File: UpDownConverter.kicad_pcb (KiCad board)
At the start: 4 copper layers, 92 parts, among them IC1 ADE-2ASK+, IC2 HMC1118LP3DE, IC3 HMC1118LP3DE, IC4 HMC1118LP3DE, IC5 ADRF5040BCPZ-R7, IC6 HMC1118LP3DE, J2 PCB.SMAFRA.HT, J3 PCB.SMAFRA.HT, J5 PCB.SMAFRA.HT, U1 AD9951

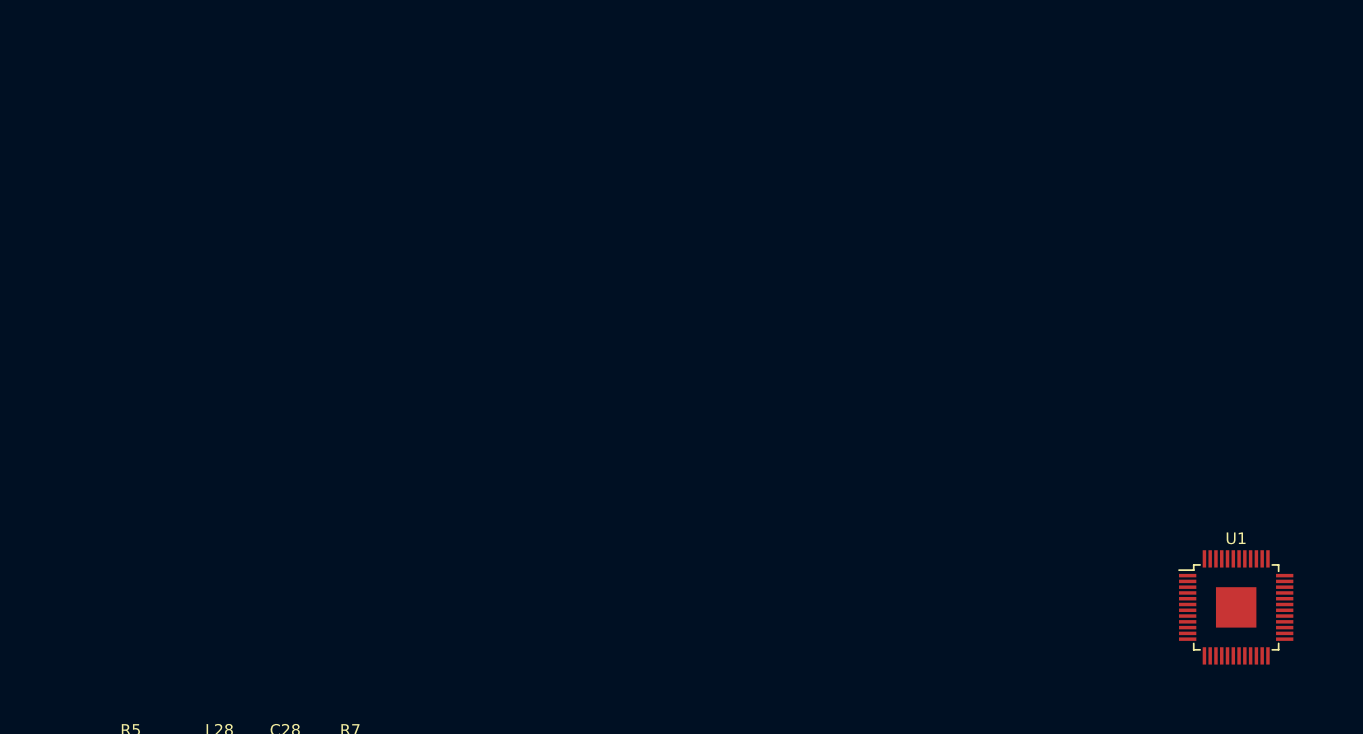
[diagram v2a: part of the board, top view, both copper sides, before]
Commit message: Replace DDS with VCOs + a switch.
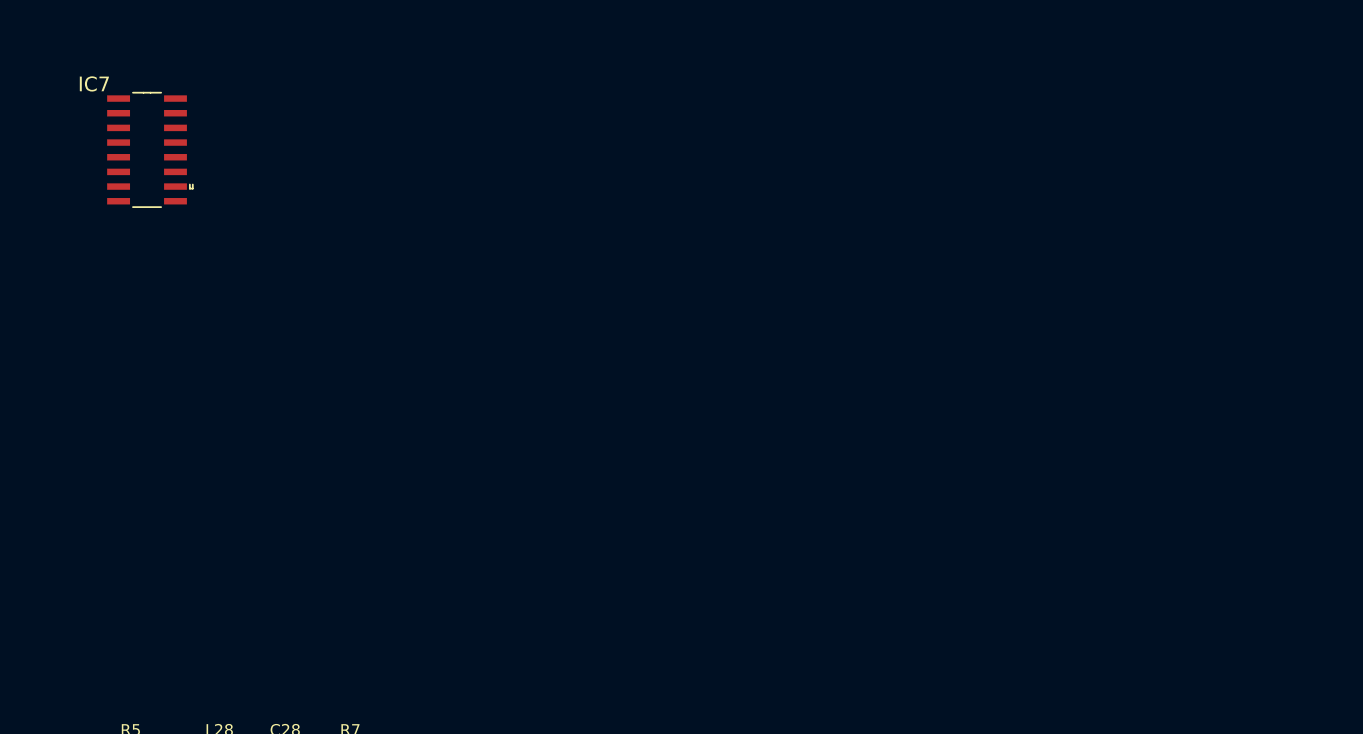
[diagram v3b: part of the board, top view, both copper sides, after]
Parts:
- removed U1: AD9951, Package_QFP:TQFP-48-1EP_7x7mm_P0.5mm_EP3.5x3.5mm
- added IC7: SN74S124D, Mouser:SOIC127P600X175-16N, F.Cu at (153.7, 84.5)
